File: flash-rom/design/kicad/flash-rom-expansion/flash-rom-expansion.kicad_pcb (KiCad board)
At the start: 2 copper layers, 73 x 45 mm, 8 parts, among them J1 Conn_01x14_Male, J2 Conn_01x14_Male, J3 Conn_01x14_Male, J4 Conn_01x16_Male, J5 Conn_01x16_Male, U1 AS6C4008-55PCN, U2 SST39SF040, U3 SST39SF040

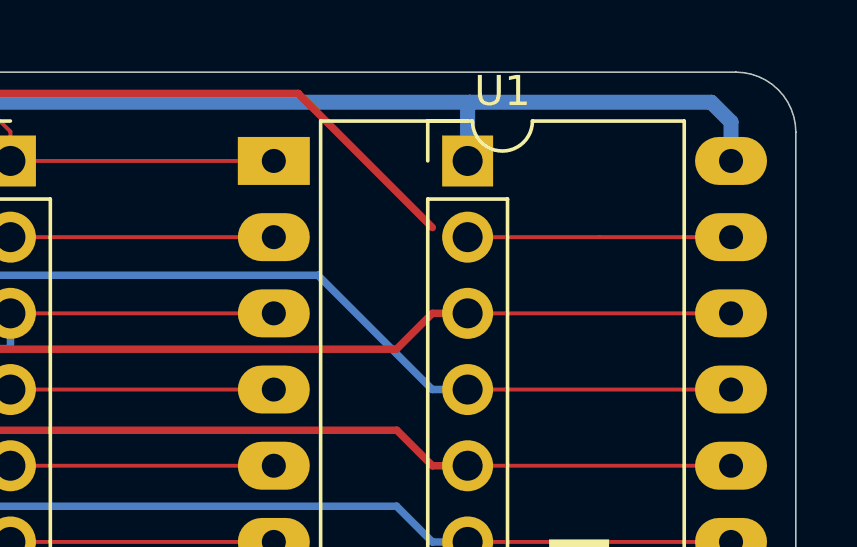
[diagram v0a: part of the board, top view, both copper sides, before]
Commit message: Fix unconnected A16 (thanks to JLCPCB for spotting)
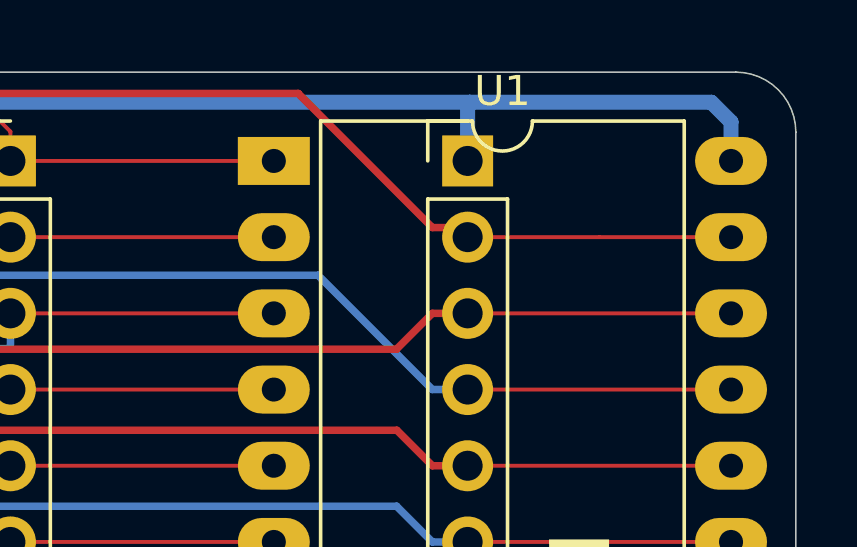
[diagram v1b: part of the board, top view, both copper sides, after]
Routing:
- net A16: track 99.5 -> 100.8 mm
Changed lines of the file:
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@@
     (thickness 1.6)
     (drawings 12)
-    (tracks 404)
+    (tracks 406)
     (zones 0)
     (modules 8)
@@
   (segment (start 73.66 65.11) (end 73.66 66.04) (width 0.13) (layer F.Cu) (net 2))
   (via (at 56.606 58.7092) (size 0.8) (layers F.Cu B.Cu) (net 2))
+  (segment (start 107.7401 63.1801) (end 108.06 63.5) (width 0.25) (layer F.Cu) (net 2))
+  (segment (start 106.8847 63.1801) (end 107.7401 63.1801) (width 0.25) (layer F.Cu) (net 2))
   (segment (start 101.6 96.52) (end 103.1253 96.52) (width 0.25) (layer B.Cu) (net 3))
   (segment (start 48.0298 101.3335) (end 49.7853 99.578) (width 0.25) (layer F.Cu) (net 3))
